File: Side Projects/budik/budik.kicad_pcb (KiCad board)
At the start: 2 copper layers, 72 parts, among them J1 Conn_01x02_Male, J2 USB_OTG, J3 FTDI, Q1 BSS138, SW1 SW_DPST_x2, SW2 SW_DPST_x2, U1 ESP-12, U2 MCP23018-E_SP, U3 uA7805, U4 LD1117S33CTR

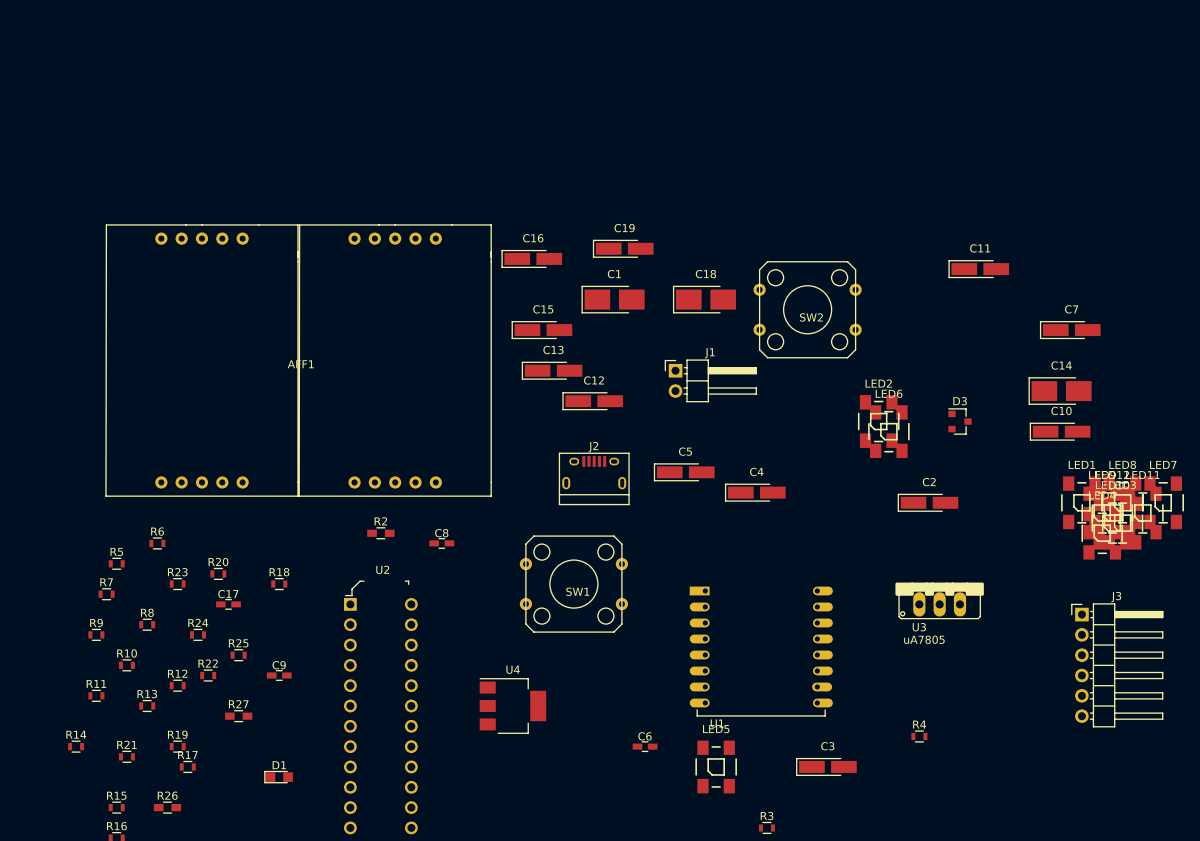
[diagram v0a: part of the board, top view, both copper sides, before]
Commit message: Arrange LEDs using the script
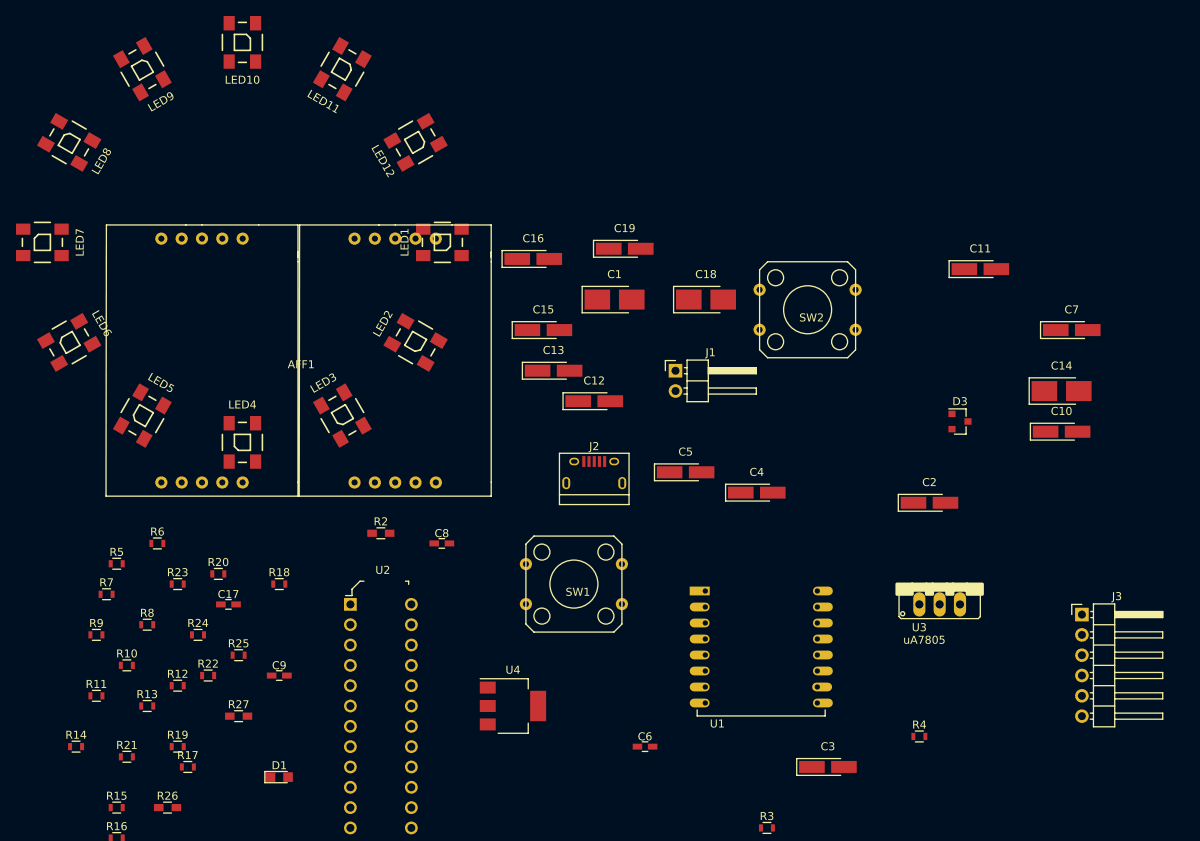
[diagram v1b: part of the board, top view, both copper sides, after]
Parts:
- moved LED7 143.8 mm to (25.0, 50.0), turned to 270 degrees
- moved LED8 139.2 mm to (28.3, 37.5), turned to 240 degrees
- moved LED9 132.2 mm to (37.5, 28.3), turned to 210 degrees
- moved LED10 124.2 mm to (50.0, 25.0), turned to 180 degrees
- moved LED11 114.4 mm to (62.5, 28.3), turned to 150 degrees
- moved LED4 108.1 mm to (50.0, 75.0)
- moved LED6 103.1 mm to (28.3, 62.5), turned to 300 degrees
- moved LED12 98.7 mm to (71.7, 37.5), turned to 120 degrees
- moved LED3 98.4 mm to (62.5, 71.7), turned to 30 degrees
- moved LED1 86.3 mm to (75.0, 50.0), turned to 90 degrees
- moved LED5 84.1 mm to (37.5, 71.7), turned to 330 degrees
- moved LED2 58.7 mm to (71.7, 62.5), turned to 60 degrees

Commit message: Add some pcb parts
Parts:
- removed R2: 300R, Resistors_SMD:R_0603_HandSoldering
- added R28: 10k, Resistors_SMD:R_0603_HandSoldering, F.Cu at (158.0, 116.3)
- added SW3: SW_SPDT, 7_segment:switch, F.Cu at (93.5, 154.4)
- C1: value 10u -> 100n
- C13: value 100n -> 10u
- C14, C18: value 10uF -> 100n
- C17, C19: value 100n -> 10uF
- R18, R20, R23: value 4k7 -> 100R
- R19, R21, R24: value 100R -> 4k7
- R26: value 10k -> 100R
- R3: value 10k -> 300R
- R5: value 150R -> 10k
- R7: value 100R -> 150R
- moved AFF1 199.4 mm to (256.5, 61.0)
- moved R13 195.4 mm to (225.6, 52.8), turned to 180 degrees
- moved R8 193.4 mm to (225.6, 50.3), turned to 180 degrees
- moved R26 192.2 mm to (225.6, 68.1), turned to 180 degrees
- moved R23 186.0 mm to (225.6, 63.0), turned to 180 degrees
- moved R22 185.1 mm to (225.6, 60.5), turned to 180 degrees
- moved R16 183.9 mm to (204.7, 55.4)
- moved R14 181.8 mm to (204.7, 65.5)
- moved R20 181.7 mm to (225.6, 57.9), turned to 180 degrees
- moved R15 180.8 mm to (204.7, 60.5)
- moved R11 179.7 mm to (204.7, 57.9)
- moved R25 179.7 mm to (225.6, 65.5), turned to 180 degrees
- moved R21 179.3 mm to (214.4, 100.6), turned to 180 degrees
- moved R9 175.7 mm to (204.7, 68.1)
- moved R18 175.0 mm to (225.6, 55.4), turned to 180 degrees
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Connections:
- C14 pad 1: +5V -> Bt1
- C15 pad 1: Net-(C15-Pad1) -> Bt2
- C16 pad 1: Net-(C16-Pad1) -> Bt3
- C17 pad 1: Net-(C17-Pad1) -> +5V
- C17 pad 2: CH_PD -> GND
- C18 pad 1: +3V3 -> Net-(C18-Pad1)
- C18 pad 2: GND -> CH_PD
- C19 pad 1: Net-(C19-Pad1) -> +3V3
- C6 pad 1: Bt1 -> Net-(C6-Pad1)
- C8 pad 1: Bt2 -> Net-(C8-Pad1)
- C9 pad 1: Bt3 -> Net-(C9-Pad1)
- D3 pad 3: Net-(C17-Pad1) -> Net-(C18-Pad1)
- J3 pad 1: Net-(C17-Pad1) -> Net-(C18-Pad1)
- LED1 pad 3: Net-(C2-Pad1) -> Net-(C1-Pad1)
- LED10 pad 3: Net-(C15-Pad1) -> Net-(C10-Pad1)
- LED11 pad 3: Net-(C16-Pad1) -> Net-(C11-Pad1)
- LED11 pad 4: Net-(LED11-Pad4) -> Net-(LED10-Pad2)
- LED12 pad 2: Net-(LED10-Pad4) -> Net-(LED12-Pad2)
- LED12 pad 3: Net-(C19-Pad1) -> Net-(C12-Pad1)
- LED2 pad 3: Net-(C3-Pad1) -> Net-(C2-Pad1)
- LED2 pad 4: Net-(LED2-Pad4) -> Net-(LED1-Pad2)
- LED3 pad 3: Net-(C4-Pad1) -> Net-(C3-Pad1)
- LED3 pad 4: Net-(LED1-Pad2) -> Net-(LED2-Pad2)
- LED4 pad 2: Net-(LED2-Pad4) -> Net-(LED4-Pad2)
- LED4 pad 3: Net-(C5-Pad1) -> Net-(C4-Pad1)
- LED4 pad 4: Net-(LED4-Pad4) -> Net-(LED3-Pad2)
- LED5 pad 3: Net-(C7-Pad1) -> Net-(C5-Pad1)
- LED5 pad 4: Net-(LED3-Pad2) -> Net-(LED4-Pad2)
- LED6 pad 2: Net-(LED4-Pad4) -> Net-(LED6-Pad2)
- LED6 pad 3: Net-(C10-Pad1) -> Net-(C6-Pad1)
- LED6 pad 4: Net-(LED6-Pad4) -> Net-(LED5-Pad2)
- LED7 pad 3: Net-(C11-Pad1) -> Net-(C7-Pad1)
- LED7 pad 4: Net-(LED5-Pad2) -> Net-(LED6-Pad2)
- LED8 pad 2: Net-(LED6-Pad4) -> Net-(LED8-Pad2)
- LED8 pad 3: Net-(C12-Pad1) -> Net-(C8-Pad1)
- LED8 pad 4: Net-(LED10-Pad2) -> Net-(LED7-Pad2)
- LED9 pad 2: Net-(LED11-Pad4) -> Net-(LED10-Pad4)
- LED9 pad 3: Net-(C13-Pad1) -> Net-(C9-Pad1)
- LED9 pad 4: Net-(LED7-Pad2) -> Net-(LED8-Pad2)
- R10 pad 1: Net-(AFF1-Pad8) -> Net-(AFF1-Pad7)
- R11 pad 1: Net-(AFF1-Pad10) -> Net-(AFF1-Pad8)
- R12 pad 1: Net-(AFF1-Pad16) -> Net-(AFF1-Pad10)
- R13 pad 1: Net-(AFF1-Pad11) -> Net-(AFF1-Pad16)
- R14 pad 1: Net-(AFF1-Pad6) -> Net-(AFF1-Pad11)
- R15 pad 1: Net-(AFF1-Pad12) -> Net-(AFF1-Pad6)
- R16 pad 1: Net-(AFF1-Pad5) -> Net-(AFF1-Pad12)
- R17 pad 1: Net-(AFF1-Pad14) -> Net-(AFF1-Pad5)
- R18 pad 1: Net-(R18-Pad1) -> Net-(AFF1-Pad14)
- R18 pad 2: GND -> Net-(R18-Pad2)
- R19 pad 1: Net-(AFF1-Pad2) -> Net-(R19-Pad1)
- R19 pad 2: Net-(R19-Pad2) -> GND
- R20 pad 1: Net-(R20-Pad1) -> Net-(AFF1-Pad2)
- R20 pad 2: GND -> Net-(R20-Pad2)
- R21 pad 1: Net-(AFF1-Pad3) -> Net-(R21-Pad1)
- R21 pad 2: Net-(R21-Pad2) -> GND
- R22 pad 1: Net-(AFF1-Pad1) -> Net-(AFF1-Pad3)
- R23 pad 1: Net-(R23-Pad1) -> Net-(AFF1-Pad1)
- R23 pad 2: GND -> Net-(R23-Pad2)
- R24 pad 2: Net-(R24-Pad2) -> GND
- R25 pad 1: Net-(AFF1-Pad15) -> Net-(AFF1-Pad13)
- R26 pad 1: GPIO0 -> Net-(AFF1-Pad15)
- R26 pad 2: +3V3 -> Net-(R26-Pad2)
- R27 pad 1: CH_PD -> GPIO0
- R3 pad 1: DATA_LED -> GND
- R3 pad 2: +3V3 -> PHOTO
- R4 pad 1: DATA_LED_5V -> DATA_LED
- R4 pad 2: +5V -> +3V3
- R5 pad 1: Net-(D1-Pad1) -> DATA_LED_5V
- R5 pad 2: GND -> +5V
- R6 pad 1: Net-(D2-Pad1) -> Net-(D1-Pad1)
- R7 pad 1: Net-(AFF1-Pad4) -> Net-(D2-Pad1)
- R7 pad 2: Net-(R7-Pad2) -> GND
- R8 pad 1: Net-(AFF1-Pad9) -> Net-(AFF1-Pad4)
- R9 pad 1: Net-(AFF1-Pad7) -> Net-(AFF1-Pad9)
- U1 pad 9: Net-(C1-Pad1) -> Net-(C13-Pad1)
- U2 pad 10: Net-(R16-Pad2) -> Net-(R17-Pad2)
- U2 pad 20: Net-(R25-Pad2) -> Net-(R26-Pad2)
- U2 pad 21: Net-(R24-Pad2) -> Net-(R25-Pad2)
- U2 pad 22: Net-(R22-Pad2) -> Net-(R23-Pad2)
- U2 pad 23: Net-(R21-Pad2) -> Net-(R22-Pad2)
- U2 pad 24: Net-(R19-Pad2) -> Net-(R20-Pad2)
- U2 pad 25: Net-(R17-Pad2) -> Net-(R18-Pad2)
- U2 pad 26: Net-(R12-Pad2) -> Net-(R13-Pad2)
- U2 pad 27: Net-(R7-Pad2) -> Net-(R8-Pad2)
- U2 pad 3: Net-(R11-Pad2) -> Net-(R12-Pad2)
- U2 pad 4: Net-(R15-Pad2) -> Net-(R16-Pad2)
- U2 pad 5: Net-(R10-Pad2) -> Net-(R11-Pad2)
- U2 pad 6: Net-(R14-Pad2) -> Net-(R15-Pad2)
- U2 pad 7: Net-(R9-Pad2) -> Net-(R10-Pad2)
- U2 pad 8: Net-(R13-Pad2) -> Net-(R14-Pad2)
- U2 pad 9: Net-(R8-Pad2) -> Net-(R9-Pad2)
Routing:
- net Net-(AFF1-Pad8): track 0.00 -> 95.7 mm, vias 0 -> 1
- net Net-(AFF1-Pad9): track 0.00 -> 89.1 mm, vias 0 -> 1
- net Net-(AFF1-Pad6): track 0.00 -> 87.4 mm, vias 0 -> 1
- net Net-(AFF1-Pad11): track 0.00 -> 87.0 mm, vias 0 -> 1
- net Net-(AFF1-Pad5): track 0.00 -> 86.3 mm, vias 0 -> 1
- net Net-(AFF1-Pad12): track 0.00 -> 82.5 mm
- net Net-(AFF1-Pad7): track 0.00 -> 81.3 mm, vias 0 -> 1
- net Net-(AFF1-Pad10): track 0.00 -> 74.1 mm
- net Net-(AFF1-Pad4): track 0.00 -> 48.4 mm, vias 0 -> 2
- net Net-(AFF1-Pad13): track 0.00 -> 42.9 mm, vias 0 -> 2
- net Net-(AFF1-Pad15): track 0.00 -> 42.6 mm, vias 0 -> 2
- net Net-(AFF1-Pad1): track 0.00 -> 33.2 mm, vias 0 -> 2
- net Net-(AFF1-Pad3): track 0.00 -> 30.7 mm, vias 0 -> 2
- net Net-(AFF1-Pad2): track 0.00 -> 30.7 mm
- net Net-(AFF1-Pad14): track 0.00 -> 25.2 mm
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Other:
- net class power added: clearance 0.2, trace_width 0.381, via_dia 0.6, via_drill 0.4

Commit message: Draw most of parts (only power missing).
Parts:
- added SW4: SW_DPST, Buttons_Switches_THT:SW_PUSH-12mm, F.Cu at (123.4, 120.9)
- added SW5: SW_DPST, Buttons_Switches_THT:SW_PUSH-12mm, F.Cu at (170.2, 77.7)
- AFF1: value DC04-11 -> DC04-11_c
- C1: footprint Capacitors_Tantalum_SMD:CP_Tantalum_Case-B_EIA-3528-21_Hand -> Capacitors_Tantalum_SMD:CP_Tantalum_Case-A_EIA-3216-18_Hand; moved to B.Cu
- C10, C11, C12, C2, C3, C4, C5, C7: moved to B.Cu
- C13: footprint Capacitors_Tantalum_SMD:CP_Tantalum_Case-A_EIA-3216-18_Hand -> Capacitors_Tantalum_SMD:CP_Tantalum_Case-B_EIA-3528-21_Hand
- C14, C18: footprint Capacitors_Tantalum_SMD:CP_Tantalum_Case-B_EIA-3528-21_Hand -> Capacitors_SMD:C_0603_HandSoldering
- C15, C16: footprint Capacitors_Tantalum_SMD:CP_Tantalum_Case-A_EIA-3216-18_Hand -> Capacitors_SMD:C_0603_HandSoldering
- C17: footprint Capacitors_SMD:C_0603_HandSoldering -> Capacitors_SMD:CP_Elec_5x5.3
- C19: footprint Capacitors_Tantalum_SMD:CP_Tantalum_Case-A_EIA-3216-18_Hand -> Capacitors_SMD:CP_Elec_5x5.3
- C6, C8, C9: footprint Capacitors_SMD:C_0603_HandSoldering -> Capacitors_Tantalum_SMD:CP_Tantalum_Case-A_EIA-3216-18_Hand; moved to B.Cu
- R26: footprint Resistors_SMD:R_0603_HandSoldering -> Resistors_SMD:R_0603
- R3: footprint Resistors_SMD:R_0603 -> Resistors_SMD:R_0603_HandSoldering
- SW1: value SW_DPST_x2 -> SW_DPST; footprint 7_segment:button_12mm -> Buttons_Switches_THT:SW_PUSH_6mm
- SW2: value SW_DPST_x2 -> SW_DPST; footprint 7_segment:button_12mm -> Buttons_Switches_THT:SW_PUSH-12mm
- moved C16 176.5 mm to (170.2, 83.3), turned to 270 degrees
- moved D2 158.6 mm to (38.1, 93.5)
- moved R7 154.2 mm to (37.1, 90.9), turned to 90 degrees
- moved C19 138.8 mm to (138.7, 111.8), turned to 180 degrees
- moved U4 137.8 mm to (142.0, 104.1), turned to 90 degrees
- moved D1 132.8 mm to (64.5, 93.5), turned to 180 degrees
- moved C15 127.8 mm to (115.3, 101.1), turned to 270 degrees
- moved R6 127.4 mm to (65.5, 90.9), turned to 90 degrees
- moved AFF1 116.8 mm to (141.7, 82.3)
- moved U2 116.8 mm to (96.5, 69.1)
- moved R10 116.8 mm to (89.9, 84.3)
- moved R11 116.8 mm to (89.9, 79.2)
- moved R12 116.8 mm to (89.9, 74.2)
- moved R13 116.8 mm to (110.7, 74.2)
- moved R14 116.8 mm to (89.9, 86.9)
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- renumbered R1 to R2
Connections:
- AFF1 pad 17: (no net) -> GND
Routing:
- net +5V: track 0.00 -> 299.2 mm, vias 0 -> 2
- net Bt3: track 0.00 -> 155.4 mm, vias 0 -> 2
- net Bt2: track 0.00 -> 133.1 mm, vias 0 -> 2
- net Bt1: track 0.00 -> 130.3 mm, vias 0 -> 2
- net CH_PD: track 7.17 -> 61.9 mm, vias 0 -> 3
- net TX: track 0.00 -> 50.5 mm
- net RX: track 0.00 -> 47.4 mm
- net DIS_SDA: track 0.00 -> 45.9 mm
- net DIS_SCL: track 0.00 -> 44.8 mm
- net GPIO0: track 4.58 -> 37.6 mm, vias 0 -> 1
- net PHOTO: track 3.81 -> 32.2 mm, vias 0 -> 1
- net DATA_LED_5V: track 0.00 -> 28.0 mm
- net GND: track 0.00 -> 21.3 mm, vias 0 -> 12
- net +3V3: track 0.00 -> 10.9 mm
- net Net-(C7-Pad1): track 2.92 -> 13.7 mm, vias 0 -> 1
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
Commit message: Finish PCB v_1.0.
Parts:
- added C20: 0.33u, Capacitors_SMD:C_0603_HandSoldering, F.Cu at (131.2, 116.0)
- added C21: 0.1u, Capacitors_SMD:C_0603_HandSoldering, F.Cu at (113.0, 119.8)
- added REF**: Test_Point_Pad_d1.0mm, Connectors_TestPoints:Test_Point_Pad_d1.0mm, F.Cu at (87.0, 112.2)
- added REF**: MountingHole_3.2mm_M3, Mounting_Holes:MountingHole_3.2mm_M3, F.Cu at (118.5, 121.0)
- added REF** (x2): MountingHole_3.2mm_M3, Mounting_Holes:MountingHole_3.2mm_M3, F.Cu at (24.0, 64.0)
- added REF**: MountingHole_3.2mm_M3, Mounting_Holes:MountingHole_3.2mm_M3, F.Cu at (79.0, 64.0)
- added REF**: MountingHole_3.2mm_M3, Mounting_Holes:MountingHole_3.2mm_M3, F.Cu at (24.0, 121.0)
- added REF**: Test_Point_Pad_d1.0mm, Connectors_TestPoints:Test_Point_Pad_d1.0mm, F.Cu at (31.5, 112.8)
- added REF**: Test_Point_Pad_d1.0mm, Connectors_TestPoints:Test_Point_Pad_d1.0mm, F.Cu at (103.2, 68.2)
- added REF**: Test_Point_Pad_d1.0mm, Connectors_TestPoints:Test_Point_Pad_d1.0mm, F.Cu at (106.5, 71.5)
- added REF**: Test_Point_Pad_d1.0mm, Connectors_TestPoints:Test_Point_Pad_d1.0mm, F.Cu at (134.2, 117.8)
- added REF**: Test_Point_Pad_d1.0mm, Connectors_TestPoints:Test_Point_Pad_d1.0mm, F.Cu at (129.2, 114.2)
- added REF**: Test_Point_Pad_d1.0mm, Connectors_TestPoints:Test_Point_Pad_d1.0mm, F.Cu at (83.5, 112.2)
- added REF**: Test_Point_Pad_d1.0mm, Connectors_TestPoints:Test_Point_Pad_d1.0mm, F.Cu at (46.0, 113.0)
- added REF**: Test_Point_Pad_d1.0mm, Connectors_TestPoints:Test_Point_Pad_d1.0mm, F.Cu at (46.0, 109.8)
- added REF**: Test_Point_Pad_d1.0mm, Connectors_TestPoints:Test_Point_Pad_d1.0mm, F.Cu at (29.0, 115.2)
- C1, C10, C11, C12, C2, C3, C4, C5, C6, C7, C8, C9: footprint Capacitors_Tantalum_SMD:CP_Tantalum_Case-A_EIA-3216-18_Hand -> Capacitors_SMD:C_0603_HandSoldering; moved to F.Cu
- C17: value 10uF -> 100n
- C19: value 10uF -> 10u
- R10, R11, R12, R13, R14, R15, R16, R17, R18, R20, R22, R23, R25, R26, R8, R9: moved to B.Cu
- U4: footprint TO_SOT_Packages_SMD:SOT-223 -> TO_SOT_Packages_SMD:ATPAK-2
- moved U4 61.6 mm to (81.8, 117.2), turned to 0 degrees
- moved SW5 60.7 mm to (120.8, 113.1)
- moved R24 60.0 mm to (125.2, 115.8), turned to 180 degrees
- moved C16 58.3 mm to (121.8, 115.8), turned to 0 degrees
- moved C19 55.5 mm to (83.2, 110.2)
- moved J3 46.3 mm to (136.6, 100.7), turned to 0 degrees
- moved D3 45.0 mm to (132.4, 100.2)
- moved C17 41.4 mm to (105.1, 120.1)
- moved C18 40.5 mm to (132.4, 103.2), turned to 180 degrees
- moved U3 29.9 mm to (128.8, 122.0)
- moved C14 27.8 mm to (92.5, 120.0), turned to 0 degrees
- moved J1 26.5 mm to (139.2, 116.8), turned to 270 degrees
- moved SW3 25.6 mm to (132.5, 113.1), turned to 90 degrees
- moved AFF1 25.0 mm to (116.8, 80.4)
- moved R21 23.2 mm to (111.8, 115.8), turned to 180 degrees
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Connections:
- R11 pad 1: Net-(AFF1-Pad8) -> Net-(AFF1-Pad11)
- R12 pad 1: Net-(AFF1-Pad10) -> Net-(AFF1-Pad12)
- R13 pad 1: Net-(AFF1-Pad16) -> Net-(AFF1-Pad14)
- R14 pad 1: Net-(AFF1-Pad11) -> Net-(AFF1-Pad6)
- R15 pad 1: Net-(AFF1-Pad6) -> Net-(AFF1-Pad9)
- R16 pad 1: Net-(AFF1-Pad12) -> Net-(AFF1-Pad10)
- R18 pad 1: Net-(AFF1-Pad14) -> Net-(AFF1-Pad15)
- R20 pad 1: Net-(AFF1-Pad2) -> Net-(AFF1-Pad13)
- R22 pad 1: Net-(AFF1-Pad3) -> Net-(AFF1-Pad4)
- R25 pad 1: Net-(AFF1-Pad13) -> Net-(AFF1-Pad3)
- R26 pad 1: Net-(AFF1-Pad15) -> Net-(AFF1-Pad2)
- R8 pad 1: Net-(AFF1-Pad4) -> Net-(AFF1-Pad16)
- R9 pad 1: Net-(AFF1-Pad9) -> Net-(AFF1-Pad8)
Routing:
- net +3V3: track 10.9 -> 136.5 mm, vias 0 -> 4
- net Bt1: track 130.3 -> 55.0 mm, vias 2 -> 0
- net Bt3: track 155.4 -> 84.1 mm, vias 2 -> 0
- net Bt2: track 133.1 -> 70.1 mm, vias 2 -> 0
- net Net-(AFF1-Pad8): track 95.7 -> 37.6 mm
- net Net-(AFF1-Pad6): track 87.4 -> 33.6 mm
- net Net-(AFF1-Pad7): track 81.3 -> 33.0 mm
- net Net-(AFF1-Pad5): track 86.3 -> 39.0 mm
- net RX: track 47.4 -> 89.9 mm, vias 0 -> 3
- net TX: track 50.5 -> 90.8 mm, vias 0 -> 3
- net GPIO0: track 37.6 -> 77.9 mm, vias 1 -> 2
- net Net-(AFF1-Pad9): track 89.1 -> 49.3 mm
- net Net-(AFF1-Pad11): track 87.0 -> 50.4 mm
- net +5V: track 299.2 -> 263.8 mm, vias 2 -> 0
- net CH_PD: track 61.9 -> 95.1 mm, vias 3 -> 2
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- added copper zone on F.Cu, net GND
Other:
- board outline added: 122 x 65 mm
- net class power removed
- board text added: "+"
- board text added: "-"
- board text added: "1"
- board text added: "BajaCali budik_v1.0 6/18"
